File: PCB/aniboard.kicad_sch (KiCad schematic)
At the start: 272 parts, among them SW1 SW_Push, SW10 SW_Push, SW11 SW_Push, SW12 SW_Push, SW13 SW_Push, SW14 SW_Push, SW15 SW_Push, SW16 SW_Push, SW17 SW_Push, SW18 SW_Push, SW19 SW_Push, SW2 SW_Push, SW20 SW_Push, SW21 SW_Push, SW22 SW_Push, SW23 SW_Push, SW24 SW_Push, SW25 SW_Push, SW26 SW_Push, SW27 SW_Push, SW28 SW_Push, SW29 SW_Push, SW3 SW_Push, SW30 SW_Push, SW31 SW_Push, SW32 SW_Push, SW33 SW_Push, SW34 SW_Push, SW35 SW_Push, SW36 SW_Push, SW37 SW_Push, SW38 SW_Push, SW39 SW_Push, SW4 SW_Push, SW40 SW_Push, SW41 SW_Push, SW42 SW_Push, SW43 SW_Push, SW44 SW_Push, SW45 SW_Push, SW46 SW_Push, SW47 SW_Push, SW48 SW_Push, SW49 SW_Push, SW5 SW_Push, SW50 SW_Push, SW51 SW_Push, SW52 SW_Push, SW53 SW_Push, SW54 SW_Push, SW55 SW_Push, SW56 SW_Push, SW57 SW_Push, SW58 SW_Push, SW59 SW_Push, SW6 SW_Push, SW60 SW_Push, SW61 SW_Push, SW62 SW_Push, SW63 SW_Push, SW64 SW_Push, SW65 SW_Push, SW66 SW_Push, SW67 SW_Push, SW68 SW_Push, SW69 SW_Push, SW7 SW_Push, SW70 SW_Push, SW71 SW_Push, SW72 SW_Push, SW73 SW_Push, SW74 SW_Push, SW75 SW_Push, SW76 SW_Push, SW77 SW_Push, SW78 SW_Push, SW79 SW_Push, SW8 SW_Push, SW80 SW_Push, SW81 SW_Push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

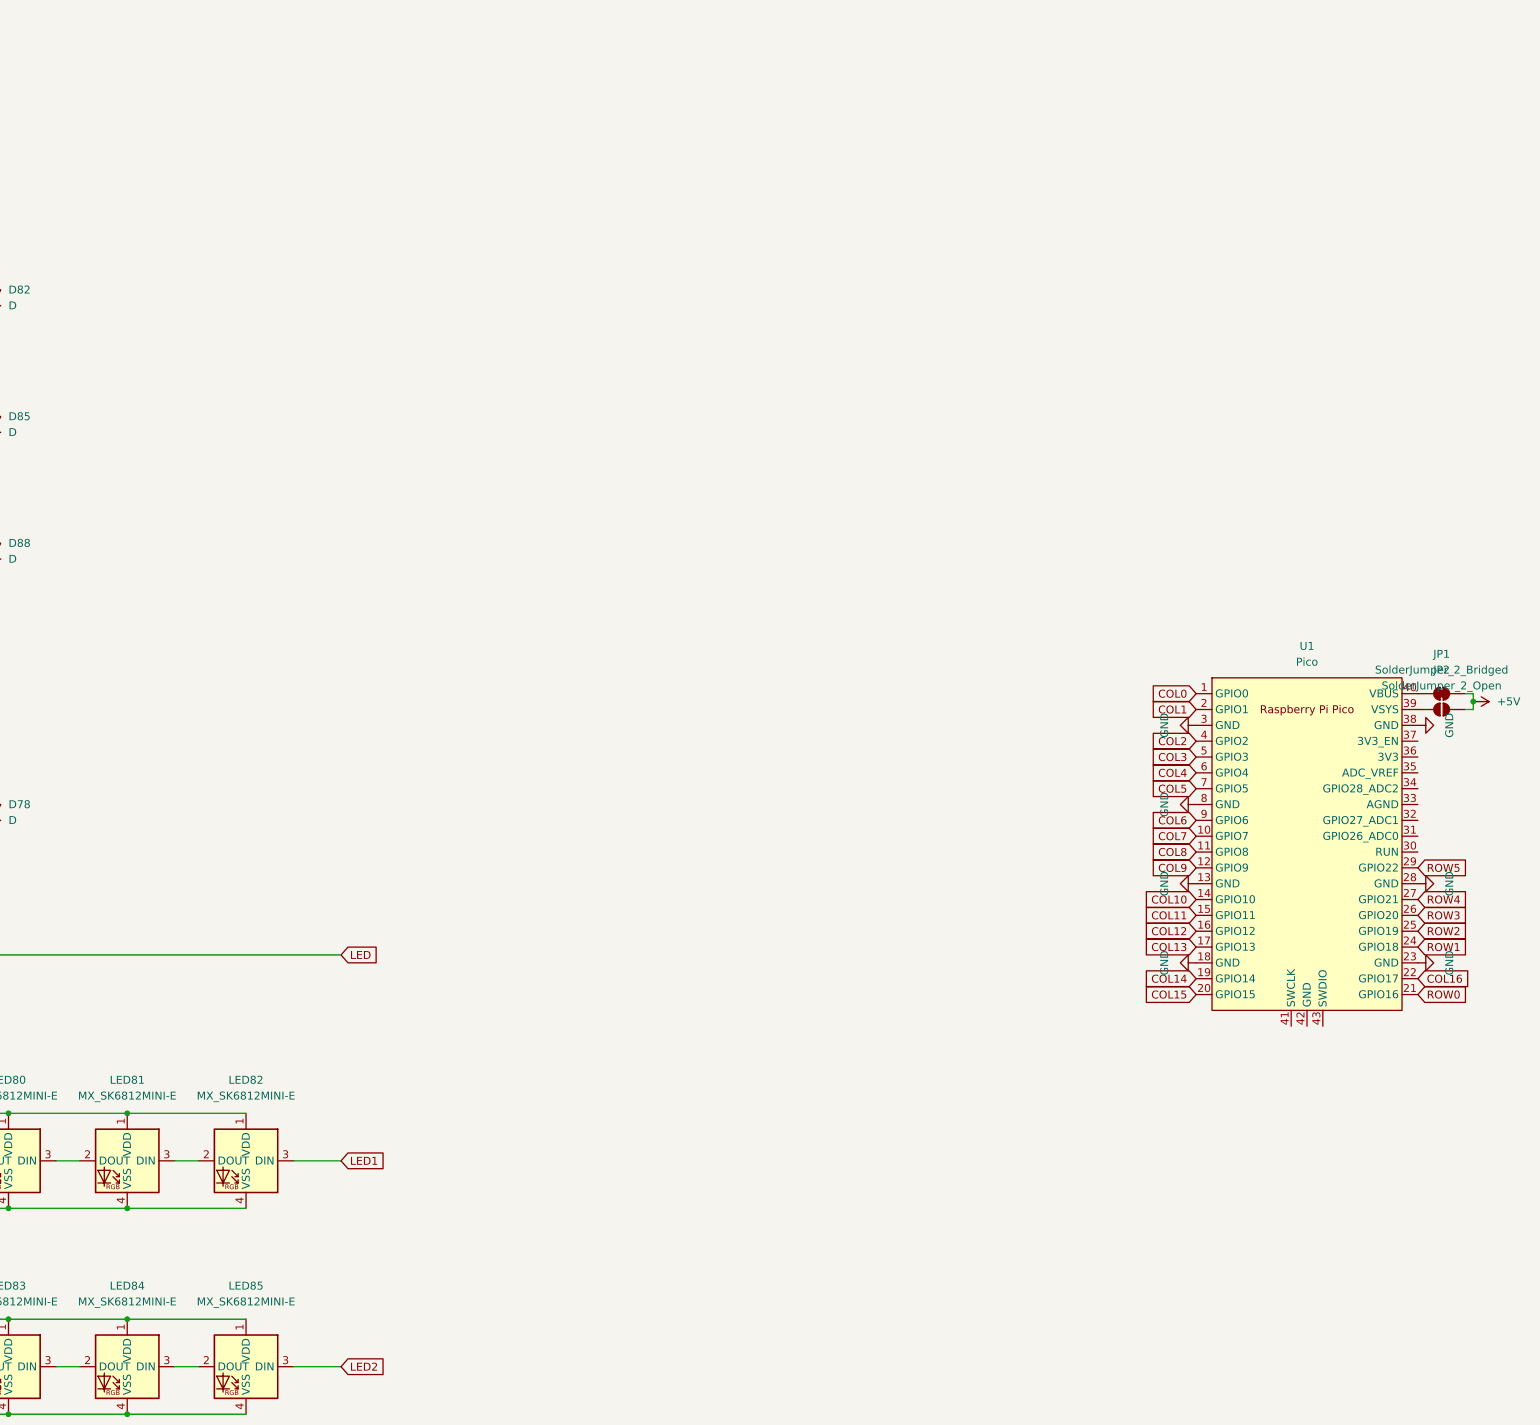
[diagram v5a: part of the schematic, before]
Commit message: Added neopixels
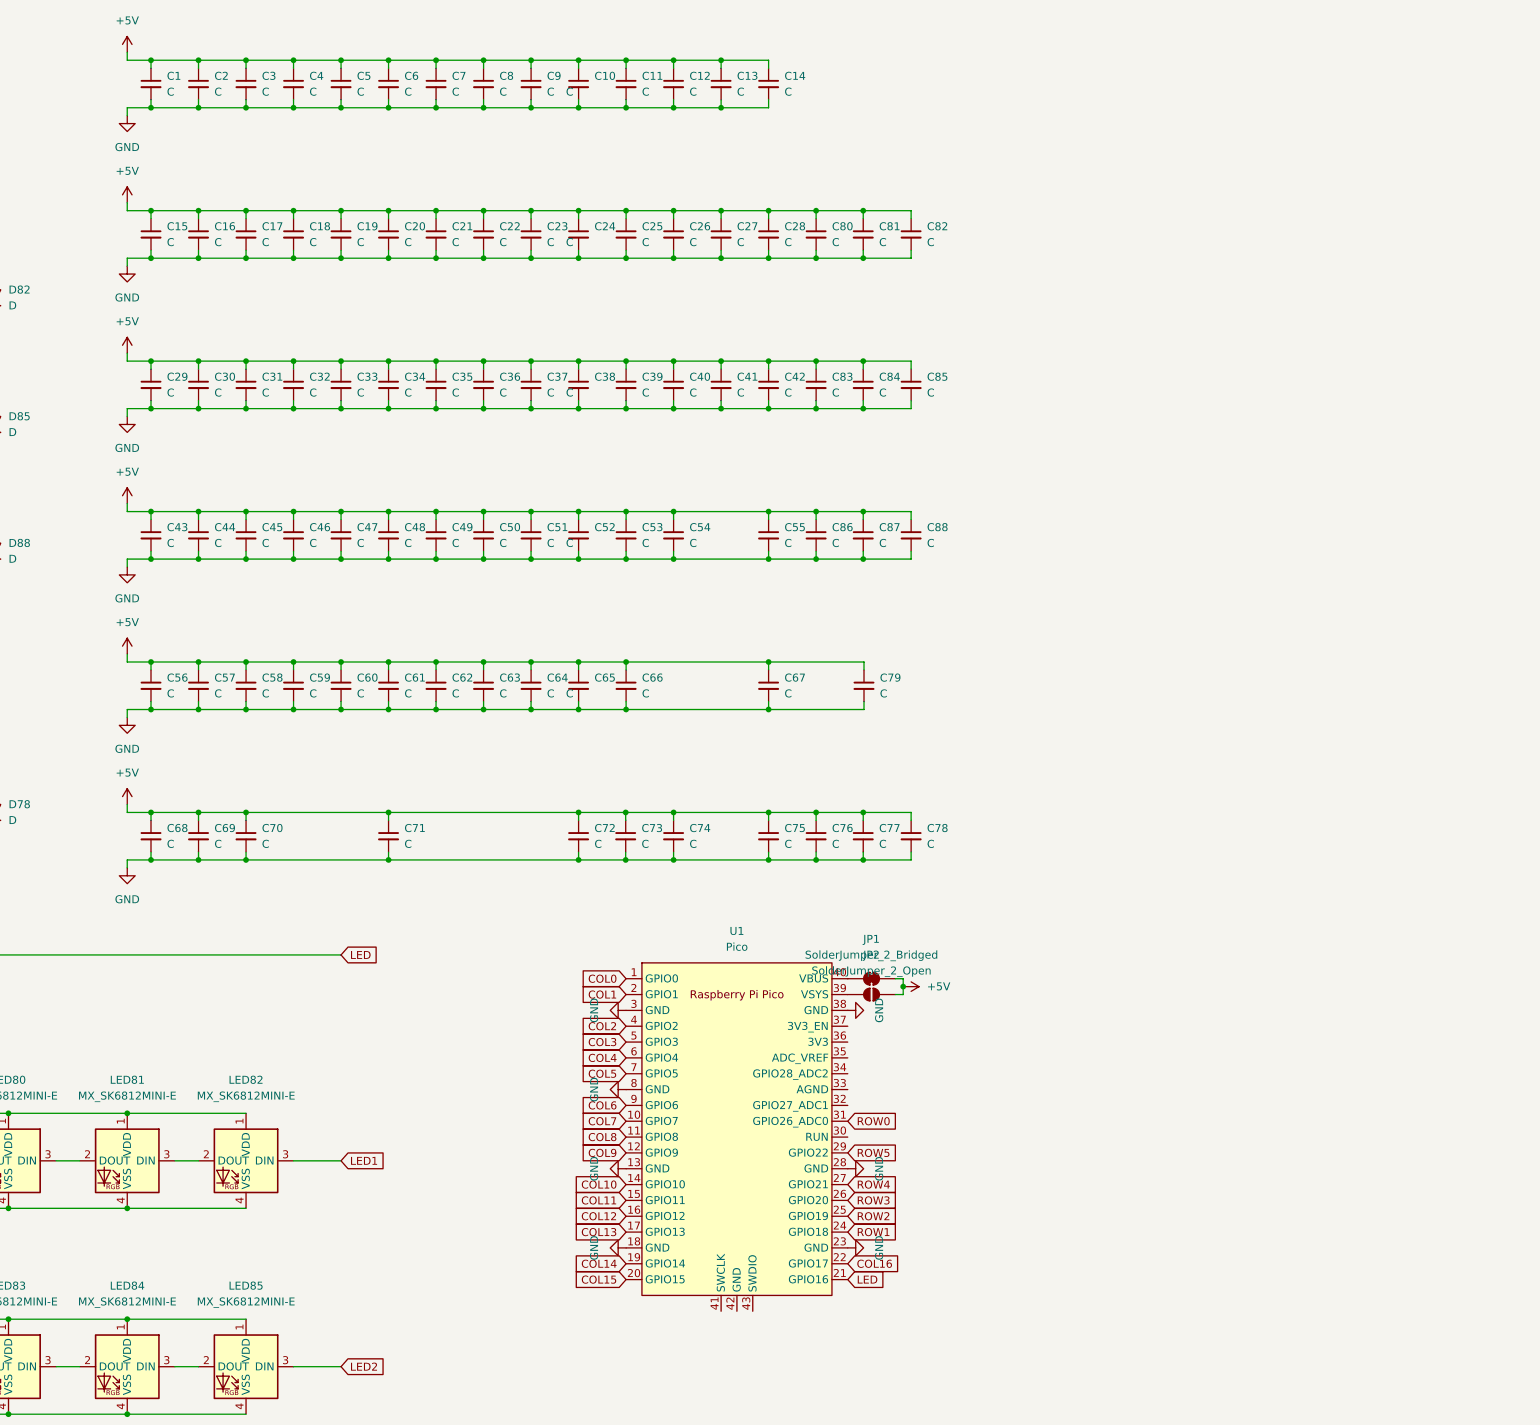
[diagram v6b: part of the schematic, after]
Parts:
- added C1, C10, C11, C12, C13, C14, C15, C16, C17, C18, C19, C2, C20, C21, C22, C23, C24, C25, C26, C27, C28, C29, C3, C30, C31, C32, C33, C34, C35, C36, C37, C38, C39, C4, C40, C41, C42, C43, C44, C45, C46, C47, C48, C49, C5, C50, C51, C52, C53, C54, C55, C56, C57, C58, C59, C6, C60, C61, C62, C63, C64, C65, C66, C67, C68, C69, C7, C70, C71, C72, C73, C74, C75, C76, C77, C78, C79, C8, C80, C81, C82, C83, C84, C85, C86, C87, C88, C9: C, Capacitor_SMD:C_0805_2012Metric_Pad1.18x1.45mm_HandSolder, symbol Device:C_Small
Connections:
- net +5V: now also C1.1, C10.1, C11.1, C12.1, C13.1, C14.1, C15.1, C16.1, C17.1, C18.1, C19.1, C2.1, C20.1, C21.1, C22.1, C23.1, C24.1, C25.1, C26.1, C27.1, C28.1, C29.1, C3.1, C30.1, C31.1, C32.1, C33.1, C34.1, C35.1, C36.1, C37.1, C38.1, C39.1, C4.1, C40.1, C41.1, C42.1, C43.1, C44.1, C45.1, C46.1, C47.1, C48.1, C49.1, C5.1, C50.1, C51.1, C52.1, C53.1, C54.1, C55.1, C56.1, C57.1, C58.1, C59.1, C6.1, C60.1, C61.1, C62.1, C63.1, C64.1, C65.1, C66.1, C67.1, C68.1, C69.1, C7.1, C70.1, C71.1, C72.1, C73.1, C74.1, C75.1, C76.1, C77.1, C78.1, C79.1, C8.1, C80.1, C81.1, C82.1, C83.1, C84.1, C85.1, C86.1, C87.1, C88.1, C9.1
- net GND: now also C1.2, C10.2, C11.2, C12.2, C13.2, C14.2, C15.2, C16.2, C17.2, C18.2, C19.2, C2.2, C20.2, C21.2, C22.2, C23.2, C24.2, C25.2, C26.2, C27.2, C28.2, C29.2, C3.2, C30.2, C31.2, C32.2, C33.2, C34.2, C35.2, C36.2, C37.2, C38.2, C39.2, C4.2, C40.2, C41.2, C42.2, C43.2, C44.2, C45.2, C46.2, C47.2, C48.2, C49.2, C5.2, C50.2, C51.2, C52.2, C53.2, C54.2, C55.2, C56.2, C57.2, C58.2, C59.2, C6.2, C60.2, C61.2, C62.2, C63.2, C64.2, C65.2, C66.2, C67.2, C68.2, C69.2, C7.2, C70.2, C71.2, C72.2, C73.2, C74.2, C75.2, C76.2, C77.2, C78.2, C79.2, C8.2, C80.2, C81.2, C82.2, C83.2, C84.2, C85.2, C86.2, C87.2, C88.2, C9.2
- net LED: now also U1.21 (GPIO16)
- net ROW0: now also U1.31 (GPIO26_ADC0); no longer U1.21 (GPIO16)
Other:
- moved on the sheet: JP1, JP2, U1

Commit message: Partial routing
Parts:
- LED15, LED16, LED17, LED18, LED19, LED20, LED21, LED22, LED23, LED24, LED25, LED26, LED27, LED28, LED43, LED44, LED45, LED46, LED47, LED48, LED49, LED50, LED51, LED52, LED53, LED54, LED55, LED68, LED69, LED70, LED71, LED72, LED73, LED74, LED75, LED76, LED77, LED78, LED80, LED81, LED82, LED86, LED87, LED88: footprint PCM_marbastlib-mx:LED_MX_6028R -> PCM_marbastlib-mx:LED_MX_6028R-ROT
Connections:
- net LED1: now also LED15.3 (DIN); no longer LED82.3 (DIN)
- net LED2: now also LED82.2 (DOUT); no longer LED15.2 (DOUT)
- net LED3: now also LED43.3 (DIN), LED88.2 (DOUT); no longer LED43.2 (DOUT), LED88.3 (DIN)
- net LED4: now also LED68.3 (DIN); no longer LED78.3 (DIN)
- net ROW3: now also D55.1 (K)
- net at LED87.2 (DOUT): now also LED88.3 (DIN); no longer LED86.3 (DIN)
- net at LED87.3 (DIN): now also LED86.2 (DOUT); no longer LED88.2 (DOUT)
- net at LED80.2 (DOUT): now also LED81.3 (DIN); no longer LED28.3 (DIN)
- net at LED80.3 (DIN): now also LED28.2 (DOUT); no longer LED81.2 (DOUT)
- net at LED78.2 (DOUT): no longer LED77.3 (DIN)
- net at LED23.2 (DOUT): now also LED24.3 (DIN); no longer LED22.3 (DIN)
- net at LED23.3 (DIN): now also LED22.2 (DOUT); no longer LED24.2 (DOUT)
- net at LED50.2 (DOUT): now also LED51.3 (DIN); no longer LED49.3 (DIN)
- net at LED50.3 (DIN): now also LED49.2 (DOUT); no longer LED51.2 (DOUT)
- net at LED44.2 (DOUT): now also LED45.3 (DIN); no longer LED43.3 (DIN)
- net at LED25.2 (DOUT): now also LED26.3 (DIN); no longer LED24.3 (DIN)
- net at LED74.2 (DOUT): now also LED75.3 (DIN); no longer LED73.3 (DIN)
- net at LED74.3 (DIN): now also LED73.2 (DOUT); no longer LED75.2 (DOUT)
- net at LED52.2 (DOUT): now also LED53.3 (DIN); no longer LED51.3 (DIN)
- net at LED72.3 (DIN): now also LED71.2 (DOUT); no longer LED73.2 (DOUT)
- net at LED46.2 (DOUT): now also LED47.3 (DIN); no longer LED45.3 (DIN)
- net at LED46.3 (DIN): now also LED45.2 (DOUT); no longer LED47.2 (DOUT)
- net at LED69.2 (DOUT): now also LED70.3 (DIN); no longer LED68.3 (DIN)
- net at LED69.3 (DIN): now also LED68.2 (DOUT); no longer LED70.2 (DOUT)
- net at LED25.3 (DIN): now also LED24.2 (DOUT); no longer LED26.2 (DOUT)
- net at LED27.2 (DOUT): now also LED28.3 (DIN); no longer LED26.3 (DIN)
- net at LED48.3 (DIN): now also LED47.2 (DOUT); no longer LED49.2 (DOUT)
- net at LED44.3 (DIN): now also LED43.2 (DOUT); no longer LED45.2 (DOUT)
- net at LED76.2 (DOUT): now also LED77.3 (DIN); no longer LED75.3 (DIN)
- net at LED20.2 (DOUT): now also LED21.3 (DIN); no longer LED19.3 (DIN)
- net at LED20.3 (DIN): now also LED19.2 (DOUT); no longer LED21.2 (DOUT)
- net at LED52.3 (DIN): now also LED51.2 (DOUT); no longer LED53.2 (DOUT)
- net at LED54.2 (DOUT): now also LED55.3 (DIN); no longer LED53.3 (DIN)
- net at LED18.3 (DIN): now also LED17.2 (DOUT); no longer LED19.2 (DOUT)
- net at LED16.2 (DOUT): now also LED17.3 (DIN); no longer LED15.3 (DIN)
- net at LED54.3 (DIN): now also LED53.2 (DOUT); no longer LED55.2 (DOUT)
- net at LED16.3 (DIN): now also LED15.2 (DOUT); no longer LED17.2 (DOUT)
- net at LED18.2 (DOUT): now also LED19.3 (DIN); no longer LED17.3 (DIN)
- net at LED27.3 (DIN): now also LED26.2 (DOUT); no longer LED28.2 (DOUT)
- net at LED72.2 (DOUT): now also LED73.3 (DIN); no longer LED71.3 (DIN)
- net at LED77.2 (DOUT): now also LED78.3 (DIN); no longer LED76.3 (DIN)
- net at LED48.2 (DOUT): now also LED49.3 (DIN); no longer LED47.3 (DIN)
- new net: LED81.2 (DOUT), LED82.3 (DIN)
- new net: LED75.2 (DOUT), LED76.3 (DIN)
- new net: LED70.2 (DOUT), LED71.3 (DIN)
- new net: LED55.2 (DOUT), LED86.3 (DIN)
- new net: LED21.2 (DOUT), LED22.3 (DIN)

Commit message: Save
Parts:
- added C89, C90: 500uf, Capacitor_THT:CP_Radial_D8.0mm_P3.50mm, symbol Device:C_Polarized
- added D89, D90: LED, symbol Device:LED
- added J1: Conn_02x03_Top_Bottom, Connector_PinHeader_2.54mm:PinHeader_2x03_P2.54mm_Vertical, symbol Connector_Generic:Conn_02x03_Top_Bottom
- added JP3: SolderJumper_2_Bridged, Jumper:SolderJumper-2_P1.3mm_Bridged_RoundedPad1.0x1.5mm, symbol Jumper:SolderJumper_2_Bridged
- added R1: 470Ω, Resistor_SMD:R_0805_2012Metric_Pad1.20x1.40mm_HandSolder, symbol Device:R
- added U2: SN74LVC1T45DBV, Package_TO_SOT_SMD:SOT-23-6, symbol Logic_LevelTranslator:SN74LVC1T45DBV
- C1, C10, C11, C12, C13, C14, C15, C16, C17, C18, C19, C2, C20, C21, C22, C23, C24, C25, C26, C27, C28, C29, C3, C30, C31, C32, C33, C34, C35, C36, C37, C38, C39, C4, C40, C41, C42, C43, C44, C45, C46, C47, C48, C49, C5, C50, C51, C52, C53, C54, C55, C56, C57, C58, C59, C6, C60, C61, C62, C63, C64, C65, C66, C67, C68, C69, C7, C70, C71, C72, C73, C74, C75, C76, C77, C78, C79, C8, C80, C81, C82, C83, C84, C85, C86, C87, C88, C9: value C -> 0.1uf
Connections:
- net +5V: now also C89.1, C90.1, U2.6 (VCCB)
- net COL0: now also U1.34 (GPIO28_ADC2); no longer U1.1 (GPIO0)
- net COL1: now also U1.32 (GPIO27_ADC1); no longer U1.2 (GPIO1)
- net COL13: no longer U1.17 (GPIO13)
- net COL14: now also U1.10 (GPIO7); no longer U1.19 (GPIO14)
- net COL15: now also U1.9 (GPIO6); no longer U1.20 (GPIO15)
- net COL16: now also U1.5 (GPIO3); no longer U1.22 (GPIO17)
- net COL2: now also U1.22 (GPIO17); no longer U1.4 (GPIO2)
- net COL3: now also U1.20 (GPIO15); no longer U1.5 (GPIO3)
- net COL4: no longer U1.6 (GPIO4)
- net COL5: no longer U1.7 (GPIO5)
- net COL6: no longer U1.9 (GPIO6)
- net COL7: no longer U1.10 (GPIO7)
- net GND: now also U1.42 (GND), C89.2, C90.2, J1.3 (Pin_3), J1.4 (Pin_4), U2.2 (GND)
- net LED: now also JP3.2 (B), U2.3 (A); no longer LED14.3 (DIN)
- net LED3: no longer LED88.2 (DOUT)
- net LED4: now also LED88.2 (DOUT); no longer LED56.2 (DOUT), LED68.3 (DIN)
- net ROW1: now also U1.4 (GPIO2); no longer U1.24 (GPIO18)
- net ROW2: now also U1.2 (GPIO1); no longer U1.25 (GPIO19)
- net ROW3: now also U1.1 (GPIO0); no longer U1.26 (GPIO20)
- net ROW4: now also U1.7 (GPIO5); no longer U1.27 (GPIO21)
- net ROW5: now also U1.6 (GPIO4); no longer U1.29 (GPIO22)
- net +3.3V: now reaches U1.36 (3V3)
- net +3.3V: now also U2.1 (VCCA), U2.5 (DIR)
- net at U1.41 (SWCLK): now also J1.5 (Pin_5)
- net at U1.43 (SWDIO): now also J1.1 (Pin_1)
- new net: JP3.1 (A), R1.2, U2.4 (B)
- new net: LED14.3 (DIN), R1.1
- new net LED5: LED56.2 (DOUT), LED68.3 (DIN)
- new net RX: J1.6 (Pin_6)
- new net TX: J1.2 (Pin_2)
- no-connect marks 0 -> 5
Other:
- note added: "Level Shifter"
- moved on the sheet: JP1, JP2, LED1, LED10, LED11, LED12, LED13, LED14, LED15, LED16, LED17, LED18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
